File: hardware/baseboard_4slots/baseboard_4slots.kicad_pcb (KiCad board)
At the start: 2 copper layers, 354 x 60 mm, 61 parts, among them J1 IO-Board_00, J10 Conn_01x04_Male, J11 Conn_01x04_Male, J12 Conn_01x04_Male, J13 Conn_01x04_Male, J14 Conn_01x04_Male, J15 Conn_02x02_Odd_Even, J2 IO-Board_01, J3 IO-Board_10, J4 IO-Board_11, J5 USB_B_Micro, J6 Conn_01x05: Adafruit 1833, J7 Screw_Terminal_01x04, J8 Conn_02x02_Odd_Even, J9 Conn_02x02_Odd_Even, U1 NRF24L01_Breakout, U2 Pico, U3 W5500_Mini

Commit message: Bump all boards to rev 0.6
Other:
- board text added: "rp2040-dmxsun USB DMX baseboard 4 slots; Rev 0.6 https://github.com/OpenLightingProject/rp2040-dmxsun"
- board text removed: "rp2040-dmxsun USB DMX baseboard 4 slots; Rev 0.5 https://github.com/OpenLightingProject/rp2040-dmxsun"
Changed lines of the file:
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@@
     (effects (font (size 1 1) (thickness 0.15)))
   )
-  (gr_text "rp2040-dmxsun USB DMX\nbaseboard 4 slots; Rev 0.5\nhttps://github.com/OpenLightingProject/rp2040-dmxsun" (at 163.2 53.5) (layer "F.SilkS")
+  (gr_text "rp2040-dmxsun USB DMX\nbaseboard 4 slots; Rev 0.6\nhttps://github.com/OpenLightingProject/rp2040-dmxsun" (at 163.2 53.5) (layer "F.SilkS")
     (effects (font (size 1 1) (thickness 0.15)))
   )

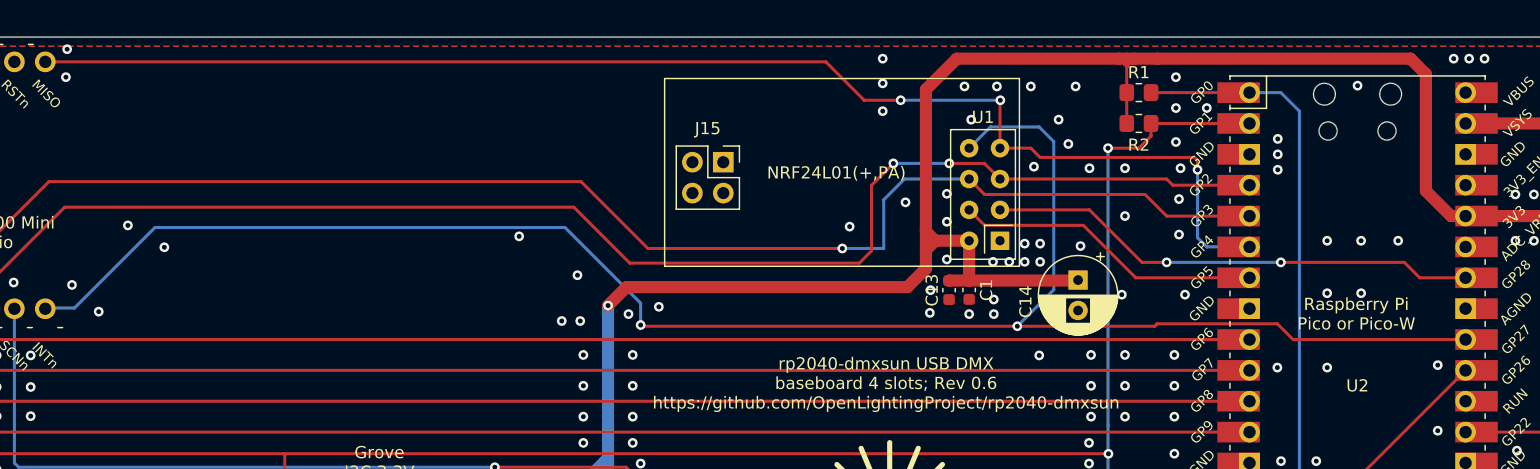
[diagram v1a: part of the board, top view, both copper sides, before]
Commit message: Hardware: Baseboard 4 slots: Don't let W5500 and nRF24 share the IRQ line, add a solder jumper instead
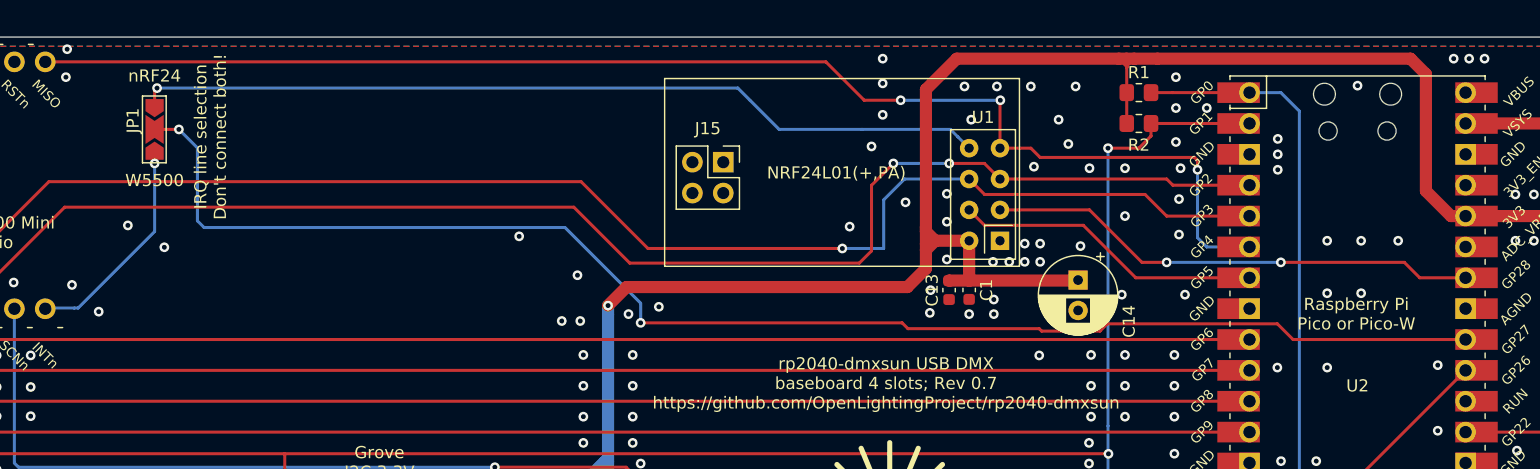
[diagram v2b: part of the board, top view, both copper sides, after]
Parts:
- added JP1: SolderJumper_3_Bridged12, Jumper:SolderJumper-3_P2.0mm_Open_TrianglePad1.0x1.5mm_NumberLabels, F.Cu at (103.0, 32.6)
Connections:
- U1 pad 8: /WIZ_NRF_INT -> /IRQ_NRF
- U2 pad 32: /WIZ_NRF_INT -> Net-(U2-Pad32)
- U3 pad 6: /WIZ_NRF_INT -> /IRQ_WIZ
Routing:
- net /WIZ_NRF_INT: track 149.1 -> 0.00 mm, vias 2 -> 0
- net Net-(U2-Pad32): track 0.00 -> 120.0 mm, vias 0 -> 2
- net /IRQ_NRF: track 0.00 -> 71.1 mm, vias 0 -> 1
- net /IRQ_WIZ: track 0.00 -> 18.7 mm, vias 0 -> 1
- net GND: vias 312 -> 313
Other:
- board text added: "IRQ line selection Don't connect both!"
- board text added: "rp2040-dmxsun USB DMX baseboard 4 slots; Rev 0.7 https://github.com/OpenLightingProject/rp2040-dmxsun"
- board text removed: "rp2040-dmxsun USB DMX baseboard 4 slots; Rev 0.6 https://github.com/OpenLightingProject/rp2040-dmxsun"

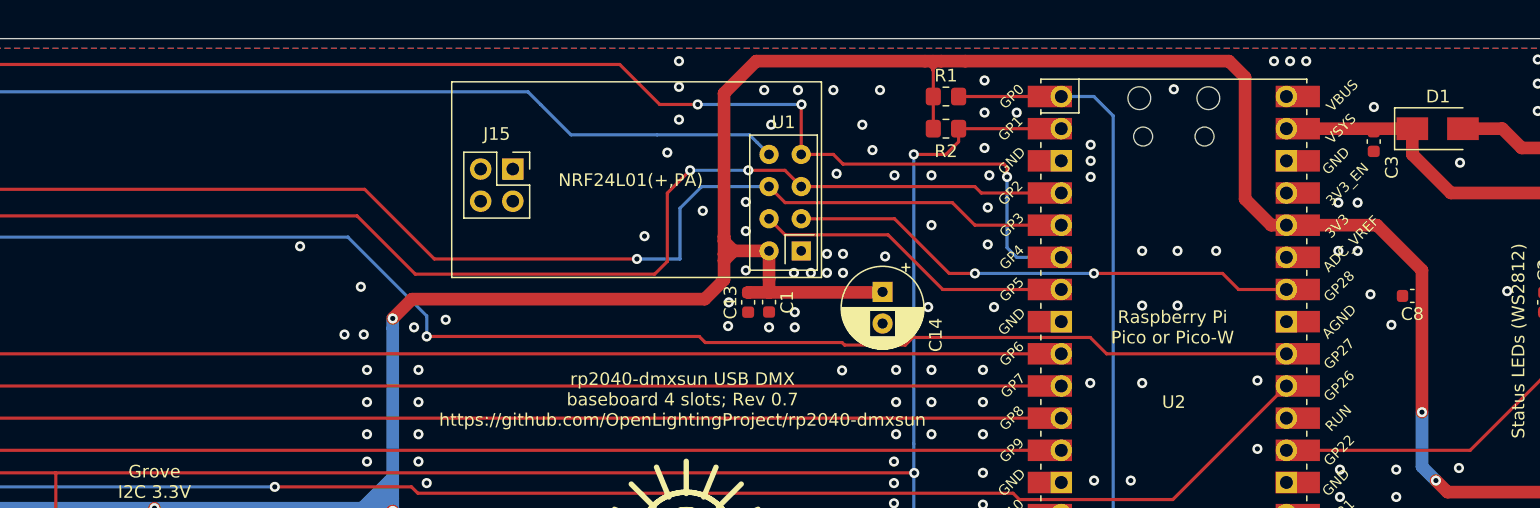
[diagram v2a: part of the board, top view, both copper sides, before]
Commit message: Update baseboards to KiCad 8, add copper keepout underneath Picos, add OpenHardware logo
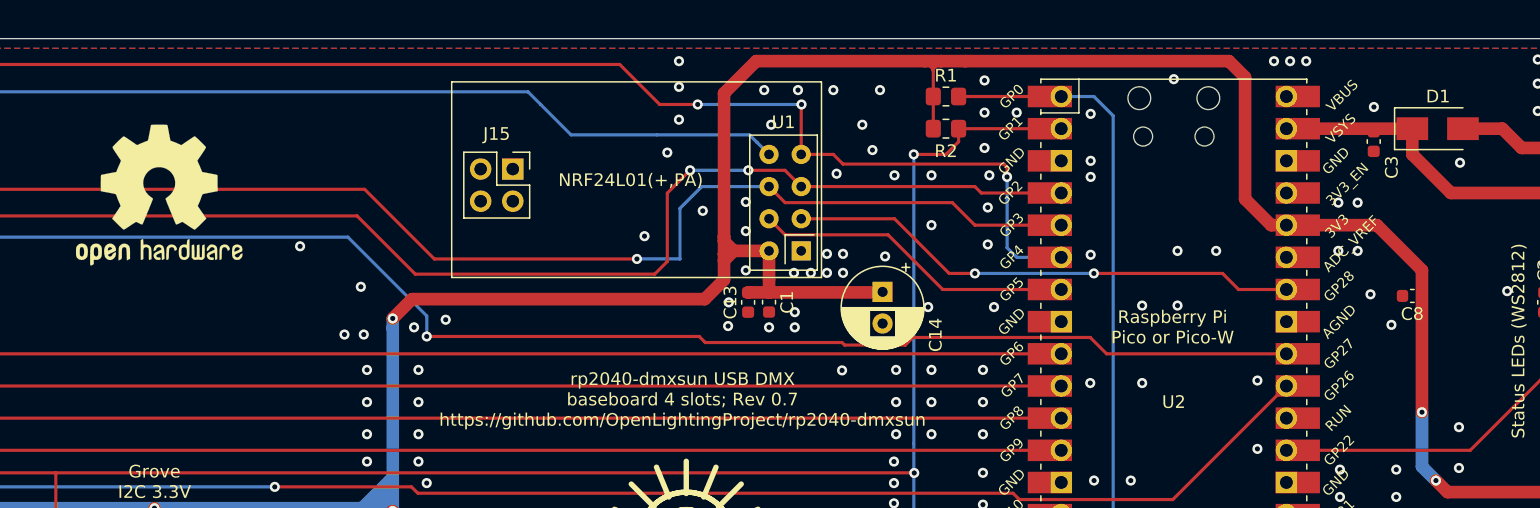
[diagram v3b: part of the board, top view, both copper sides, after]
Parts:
- added SYM1: Logo_Open_Hardware_Large, Symbol:OSHW-Logo2_14.6x12mm_SilkScreen, F.Cu at (121.9, 37.3)
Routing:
- net GND: vias 313 -> 314

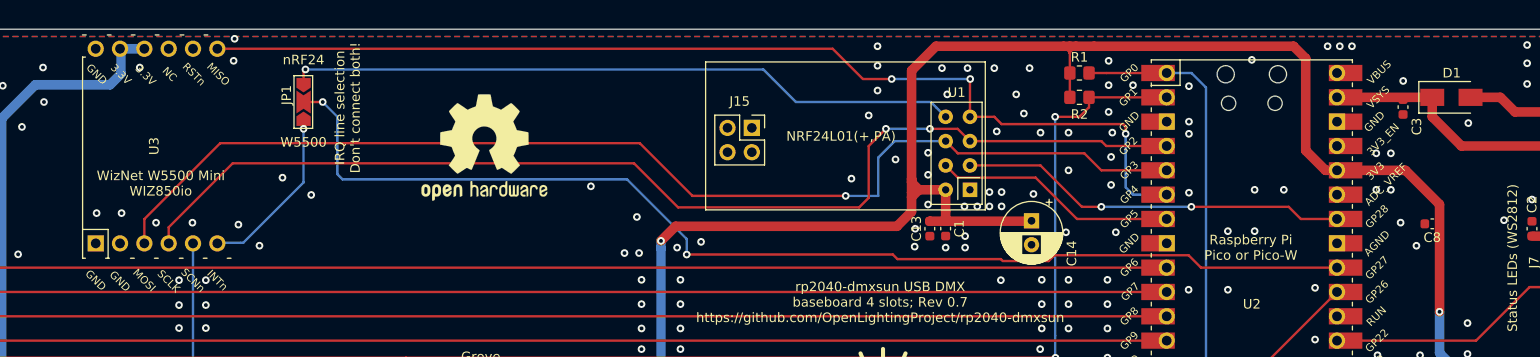
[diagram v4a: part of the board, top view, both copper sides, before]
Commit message: Update all footprints and ignore all other DRC warning on baseboards
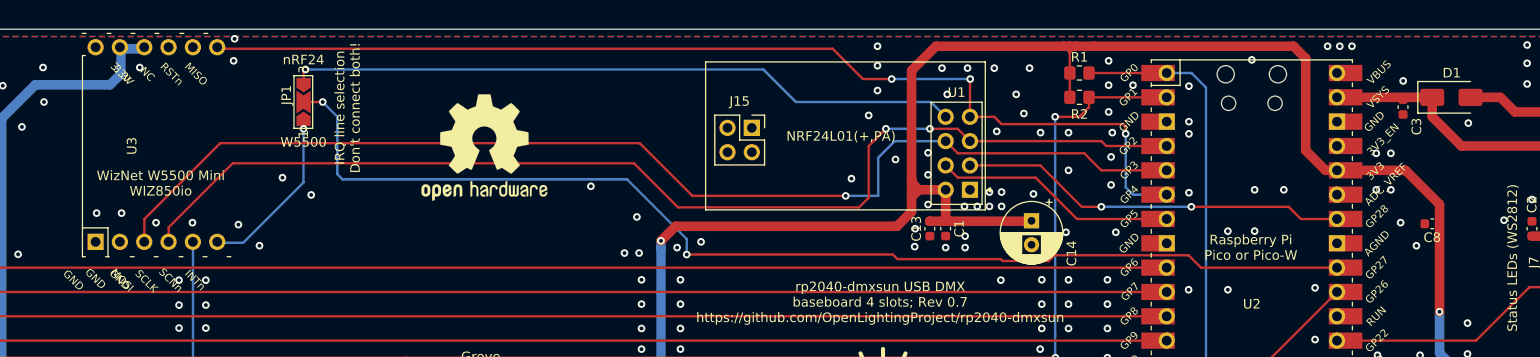
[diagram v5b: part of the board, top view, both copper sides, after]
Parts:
- moved U3 2.31 mm to (85.1, 37.2)
